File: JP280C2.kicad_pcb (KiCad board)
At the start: 2 copper layers, 160 x 44 mm, 11 parts, among them J1 Ribbon Cable (A), J2 Ribbon Cable (B), J3 Meters

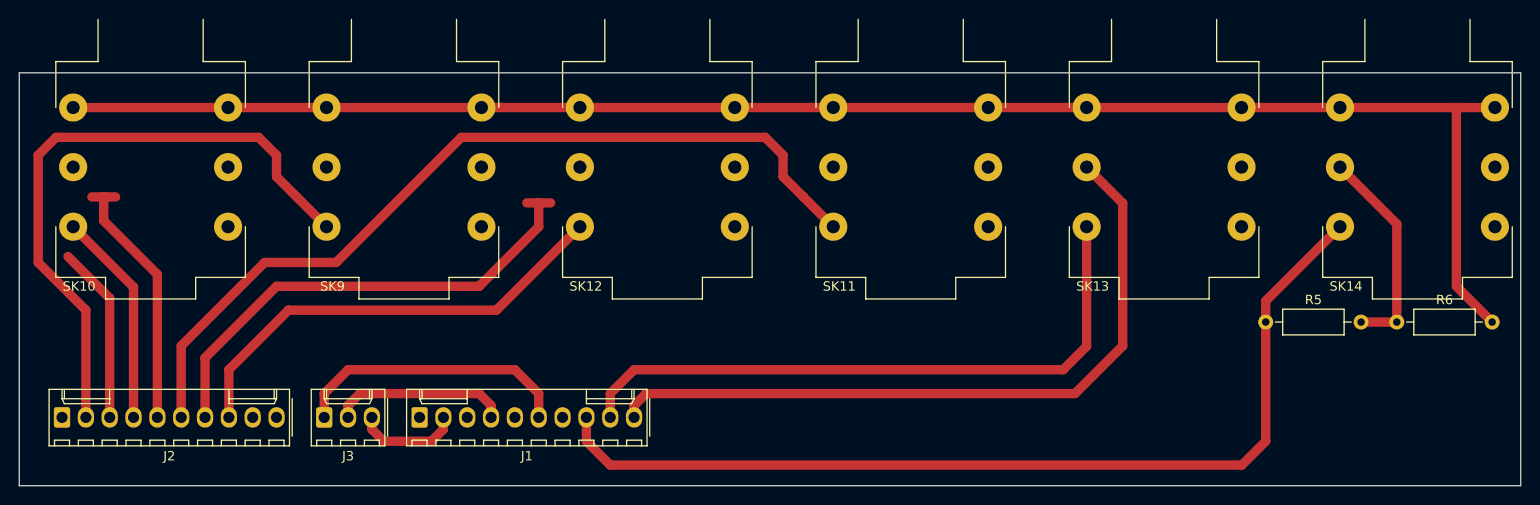
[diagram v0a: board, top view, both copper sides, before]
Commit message: part of copper pour
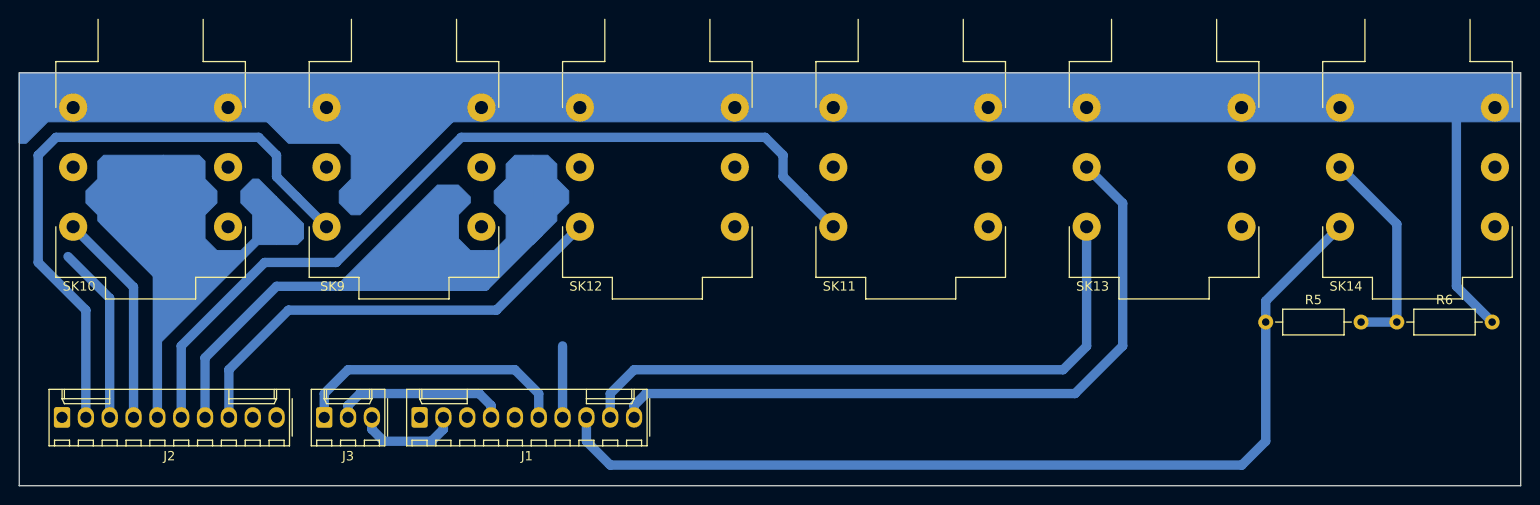
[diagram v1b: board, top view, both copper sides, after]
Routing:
- net Net-(J1-Pad7): track 0.00 -> 7.62 mm
- net Net-(J2-Pad5): track 28.4 -> 23.3 mm

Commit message: completed copper pour
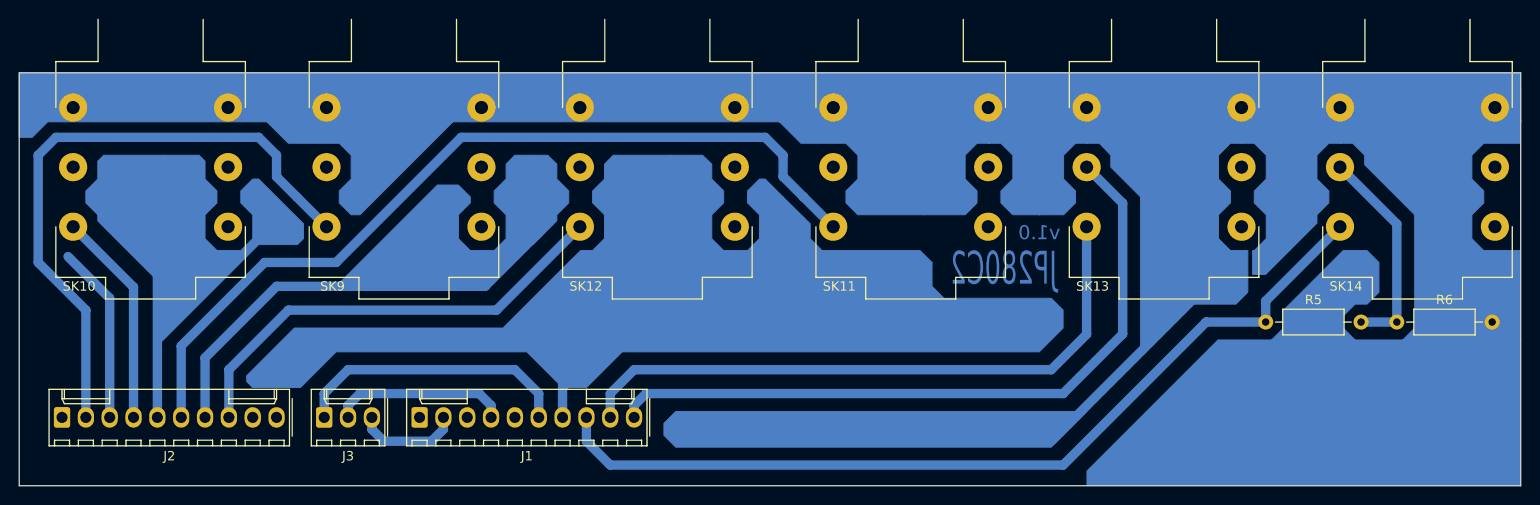
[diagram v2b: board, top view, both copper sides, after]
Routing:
- net (no net): track 0.00 -> 21.6 mm
- net Net-(J1-Pad8): track 103.2 -> 95.7 mm
- net Net-(J1-Pad7): track 7.62 -> 9.53 mm
- net Net-(J1-Pad9): track 68.1 -> 67.4 mm
- net Net-(J1-Pad10): track 76.6 -> 75.9 mm
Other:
- board text added: "JP280C2"
- board text added: "v1.0"
